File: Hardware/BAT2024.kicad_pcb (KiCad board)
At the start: 2 copper layers, 60 x 60 mm, 55 parts, among them IC1 BGM220PC22WGA2R, IC2 EEPROM_M95P16-IXMNT_E, IC3 LED-Driver_LP55231SQX_NOPB, J1 Conn_ARM_SWD_TagConnect_TC203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, J2 USB4105-GF-A-060, U1 MIC5504-3.3YM5, U2 BQ21040DBVR

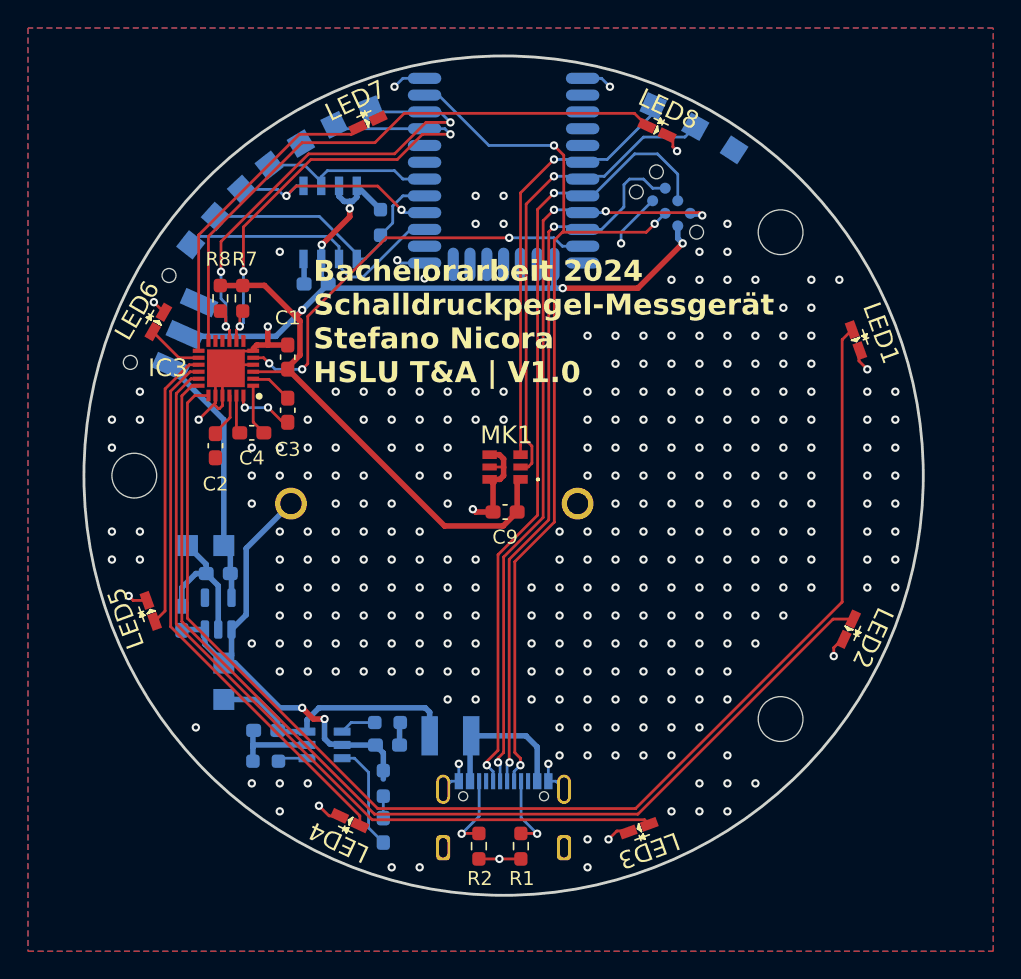
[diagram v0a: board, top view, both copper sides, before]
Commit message: Removed most vias for stitching, minor general adjustments for layout
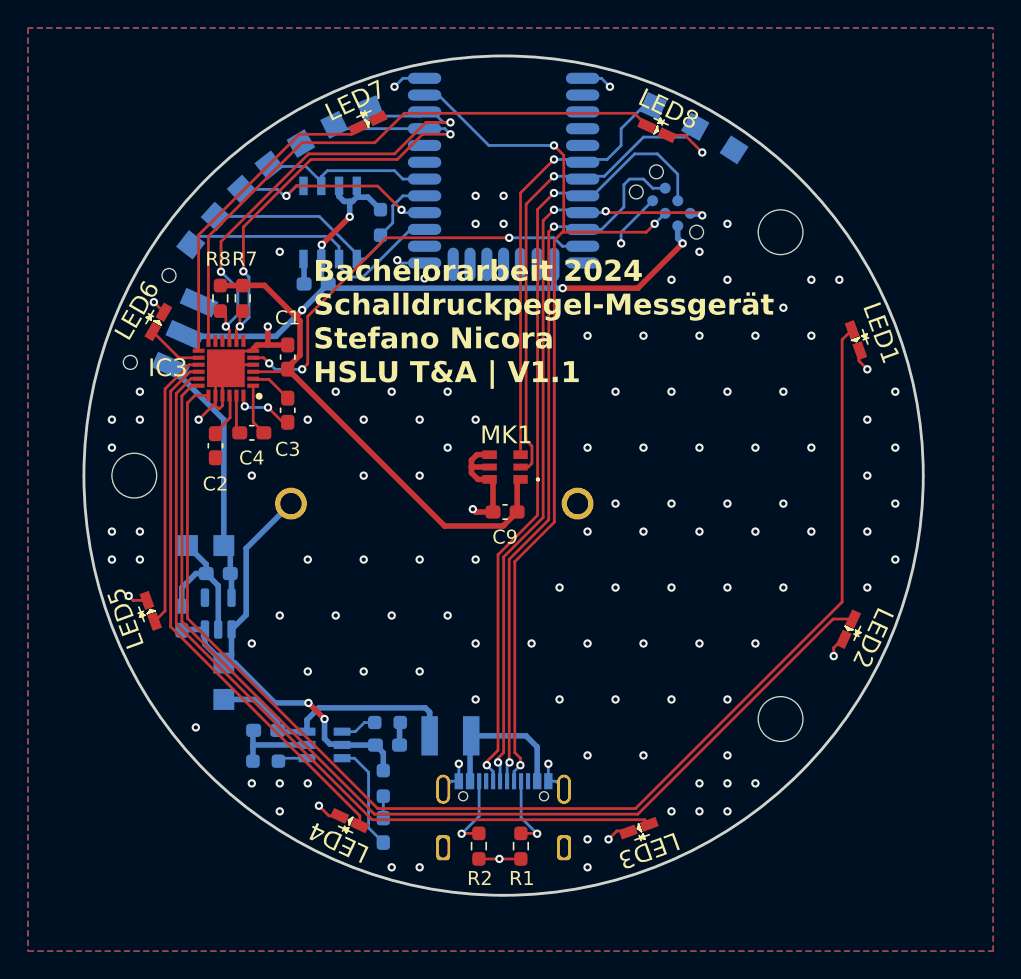
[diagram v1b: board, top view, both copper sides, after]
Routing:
- net GND: track 75.2 -> 77.5 mm, vias 294 -> 126
- net /I2C_SCL: track 34.7 -> 35.6 mm
- net +BATT: track 34.8 -> 34.2 mm
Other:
- board text added: "Bachelorarbeit 2024 Schalldruckpegel-Messgerät Stefano Nicora HSLU T&A | V1.1"
- board text removed: "Bachelorarbeit 2024 Schalldruckpegel-Messgerät Stefano Nicora HSLU T&A | V1.0"

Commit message: Created PCB V1-2; see documentation for changelog
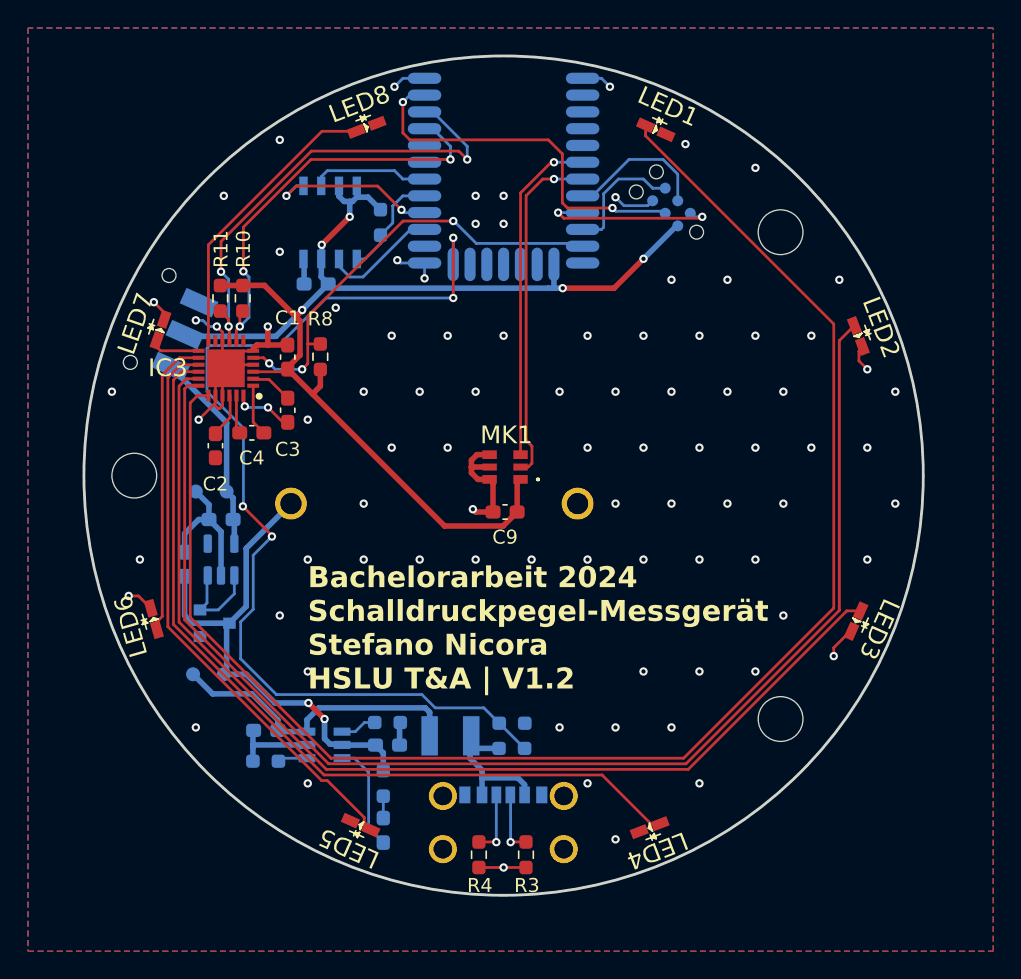
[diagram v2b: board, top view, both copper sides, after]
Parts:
- removed the J2 at (114.2, 83.9)
- removed TP10: MOSI, BAT_Footprint-Library:TestPoint_Pad_1.5x1.5mm
- removed TP11: MISO, BAT_Footprint-Library:TestPoint_Pad_1.5x1.5mm
- removed TP12: CLK, BAT_Footprint-Library:TestPoint_Pad_1.5x1.5mm
- removed TP13: PDM_CLK, BAT_Footprint-Library:TestPoint_Pad_1.5x1.5mm
- removed TP14: PDM_DATA0, BAT_Footprint-Library:TestPoint_Pad_1.5x1.5mm
- removed TP5, TP6: GND, BAT_Footprint-Library:TestPoint_Pad_1.5x1.5mm
- removed TP7: SDA, BAT_Footprint-Library:TestPoint_Pad_1.5x1.5mm
- removed TP8: SCL, BAT_Footprint-Library:TestPoint_Pad_1.5x1.5mm
- removed TP9: CS, BAT_Footprint-Library:TestPoint_Pad_1.5x1.5mm
- added J1: USB4125-GF-A, BAT_Footprint-Library:USB4125GFA, B.Cu at (114.2, 82.9)
- added Q1: SSM3J334R,LF, BAT_Footprint-Library:SSM3J334RLF, B.Cu at (93.6, 67.9)
- added R1: 10k, Resistor_SMD:R_0603_1608Metric_Pad0.98x0.95mm_HandSolder, B.Cu at (114.8, 76.8)
- added R2: 10k, Resistor_SMD:R_0603_1608Metric_Pad0.98x0.95mm_HandSolder, B.Cu at (114.8, 75.0)
- added R8: 10k, Resistor_SMD:R_0603_1608Metric_Pad0.98x0.95mm_HandSolder, F.Cu at (101.1, 48.8)
- TP1, TP2, TP3, TP4: footprint BAT_Footprint-Library:TestPoint_Pad_1.5x1.5mm -> BAT_Footprint-Library:TestPoint_Pad_D1.0mm
- moved TP4 45.6 mm to (92.2, 58.5), turned to 0 degrees
- moved LED3 21.5 mm to (139.4, 67.7), turned to 66 degrees
- moved LED4 21.4 mm to (124.7, 82.5), turned to 21 degrees
- moved LED5 21.4 mm to (104.0, 82.3), turned to -24 degrees
- moved LED6 21.2 mm to (89.2, 67.6), turned to -74 degrees
- moved LED2 21.0 mm to (139.6, 47.3), turned to 111 degrees
- moved LED7 21.0 mm to (89.7, 46.9), turned to -109 degrees
- moved LED1 20.8 mm to (125.1, 32.6), turned to 156 degrees
- moved LED8 20.8 mm to (104.4, 32.4), turned to -159 degrees
- moved C7 3.87 mm to (91.4, 63.7)
- moved C8 3.87 mm to (94.0, 60.5)
- moved TP3 3.87 mm to (94.4, 58.5)
- moved U1 3.87 mm to (94.0, 63.3)
- moved TP1 2.84 mm to (92.0, 71.5)
- moved TP2 0.80 mm to (94.2, 71.5)
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- renumbered J1 to J2, R7 to R10, R8 to R11, R1 to R3, R2 to R4, R3 to R5, R4 to R6, R5 to R7, R6 to R9
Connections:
- IC1 pad 19: unconnected-(IC1-PD02-Pad19) -> /Charge
- IC3 pad 10: unconnected-(IC3-TRIG-Pad10) -> GND
- U1 pad 1: +BATT -> Net-(U1-EN)
- U1 pad 3: +BATT -> Net-(U1-EN)
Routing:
- net /Charge: track 0.00 -> 73.3 mm, vias 0 -> 4
- net /SWCLK: track 56.7 -> 10.1 mm, vias 2 -> 0
- net /SWO: track 51.8 -> 9.07 mm, vias 2 -> 0
- net /SWDIO: track 54.3 -> 13.4 mm, vias 4 -> 2
- net /RESET: track 66.2 -> 27.1 mm, vias 3 -> 2
- net /LED8: track 42.8 -> 20.8 mm
- net /LED4: track 39.2 -> 60.2 mm
- net /LED5: track 20.0 -> 41.0 mm
- net /LED7: track 22.8 -> 3.57 mm
- net /LED3: track 58.3 -> 76.3 mm
- net /LED6: track 4.06 -> 21.5 mm
- net /LED2: track 77.1 -> 94.0 mm
- net /LED1: track 95.4 -> 111.6 mm
- net /SPI_MISO: track 20.4 -> 8.36 mm
- net /SPI_CS: track 19.3 -> 7.77 mm
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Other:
- board text added: "3V3"
- board text added: "BAT"
- board text added: "Bachelorarbeit 2024 Schalldruckpegel-Messgerät Stefano Nicora HSLU T&A | V1.2"
- board text added: "EIN"
- board text added: "USB"
- board text removed: "Bachelorarbeit 2024 Schalldruckpegel-Messgerät Stefano Nicora HSLU T&A | V1.1"
- board text removed: "CS"
- board text removed: "DATA0"
- board text removed: "MISO"
- board text removed: "MOSI"
- board text removed: "SCK"
- board text removed: "SCL"
- board text removed: "SDA"
